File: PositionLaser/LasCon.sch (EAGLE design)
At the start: 10 parts

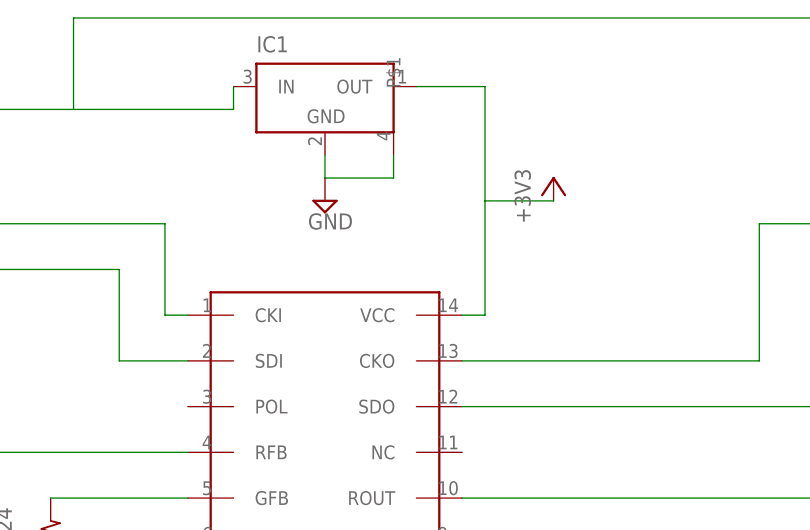
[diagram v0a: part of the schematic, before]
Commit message: Finished laser layout
Had to use one via. Will try and optimize it out later
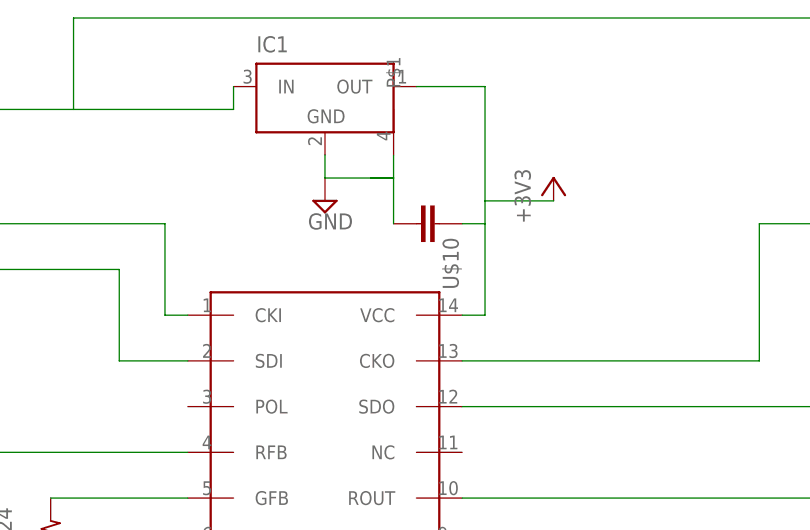
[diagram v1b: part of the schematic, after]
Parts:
- added U$10: (no value), GW-devices:RF-C0805
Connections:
- net +3V3: now also U$10.1
- net GND: now also U$10.2
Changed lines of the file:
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@@
 <part name="U$8" library="GW-devices" deviceset="90DEGMNT" device=""/>
 <part name="U$9" library="GW-devices" deviceset="90DEGMNT" device=""/>
+<part name="U$10" library="GW-devices" deviceset="RF-C" device="0805"/>
 </parts>
 <sheets>
@@
 <instance part="U$8" gate="G$1" x="-60.96" y="-53.34"/>
 <instance part="U$9" gate="G$1" x="119.38" y="-53.34"/>
+<instance part="U$10" gate="G$1" x="25.4" y="5.08" rot="R270"/>
 </instances>
 <busses>
@@
 <wire x1="12.7" y1="10.16" x2="12.7" y2="12.7" width="0.1524" layer="91"/>
 <pinref part="IC1" gate="G$1" pin="P$1"/>
-<wire x1="12.7" y1="10.16" x2="20.32" y2="10.16" width="0.1524" layer="91"/>
+<wire x1="12.7" y1="10.16" x2="17.78" y2="10.16" width="0.1524" layer="91"/>
+<wire x1="17.78" y1="10.16" x2="20.32" y2="10.16" width="0.1524" layer="91"/>
 <wire x1="20.32" y1="10.16" x2="20.32" y2="12.7" width="0.1524" layer="91"/>
+<pinref part="U$10" gate="G$1" pin="2"/>
+<wire x1="17.78" y1="10.16" x2="20.32" y2="10.16" width="0.1524" layer="91"/>
+<wire x1="20.32" y1="10.16" x2="20.32" y2="5.08" width="0.1524" layer="91"/>
 </segment>
 <segment>
@@
 <wire x1="30.48" y1="20.32" x2="30.48" y2="7.62" width="0.1524" layer="91"/>
 <pinref part="U$3" gate="G$1" pin="VCC"/>
-<wire x1="30.48" y1="7.62" x2="30.48" y2="-5.08" width="0.1524" layer="91"/>
+<wire x1="30.48" y1="7.62" x2="30.48" y2="5.08" width="0.1524" layer="91"/>
+<wire x1="30.48" y1="5.08" x2="30.48" y2="-5.08" width="0.1524" layer="91"/>
 <wire x1="30.48" y1="-5.08" x2="27.94" y2="-5.08" width="0.1524" layer="91"/>
 <pinref part="IC1" gate="G$1" pin="OUT"/>
 <pinref part="+3V1" gate="G$1" pin="+3V3"/>
 <wire x1="38.1" y1="7.62" x2="30.48" y2="7.62" width="0.1524" layer="91"/>
+<pinref part="U$10" gate="G$1" pin="1"/>
+<wire x1="27.94" y1="5.08" x2="30.48" y2="5.08" width="0.1524" layer="91"/>
 </segment>
 </net>
